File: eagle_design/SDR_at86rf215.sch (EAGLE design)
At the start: 221 parts, among them CON1 1734035-2, J1 SI-50170, J2 SJ-3523, J3 SMA0.062, J4 AMPHENOL_A-1JB, J5 5027740891, J6 AMPHENOL_A-1JB, J8 TC2030-CTX, Q1 MAR6-SM+, Q16 2N7002, SW1 45X45MM_TL3315, SW2 45X45MM_TL3315, SW3 45X45MM_TL3315, SW4 45X45MM_TL3315, SW5 45X45MM_TL3315, SW6 45X45MM_TL3315, SW7 45X45MM_TL3315, T1 0896FB15A0100, U1 AT86RF215, U10 NHD-C0216CZ-NSW-BBW-3V3, U11 MP34DT05TR-A, U12 ADP7156ARDZ-3.3-R7, U13 SN65LVDS1, U14 SN65LVDS1, U15 SN65LVDT2, U18 LAN8742, U2 ICE40HX8K-CT256, U3 TPS799X, U4 LD1117S12TR, U5 SN65LVDT2, U6 SN65LVDT2, U7 CS4344, U8 FT230XQ, U9 STM32H743ZIT6, X1 25MHz, X2 8MHZ, X3 ASVTX-12-A-40.000MHZ-H10-T

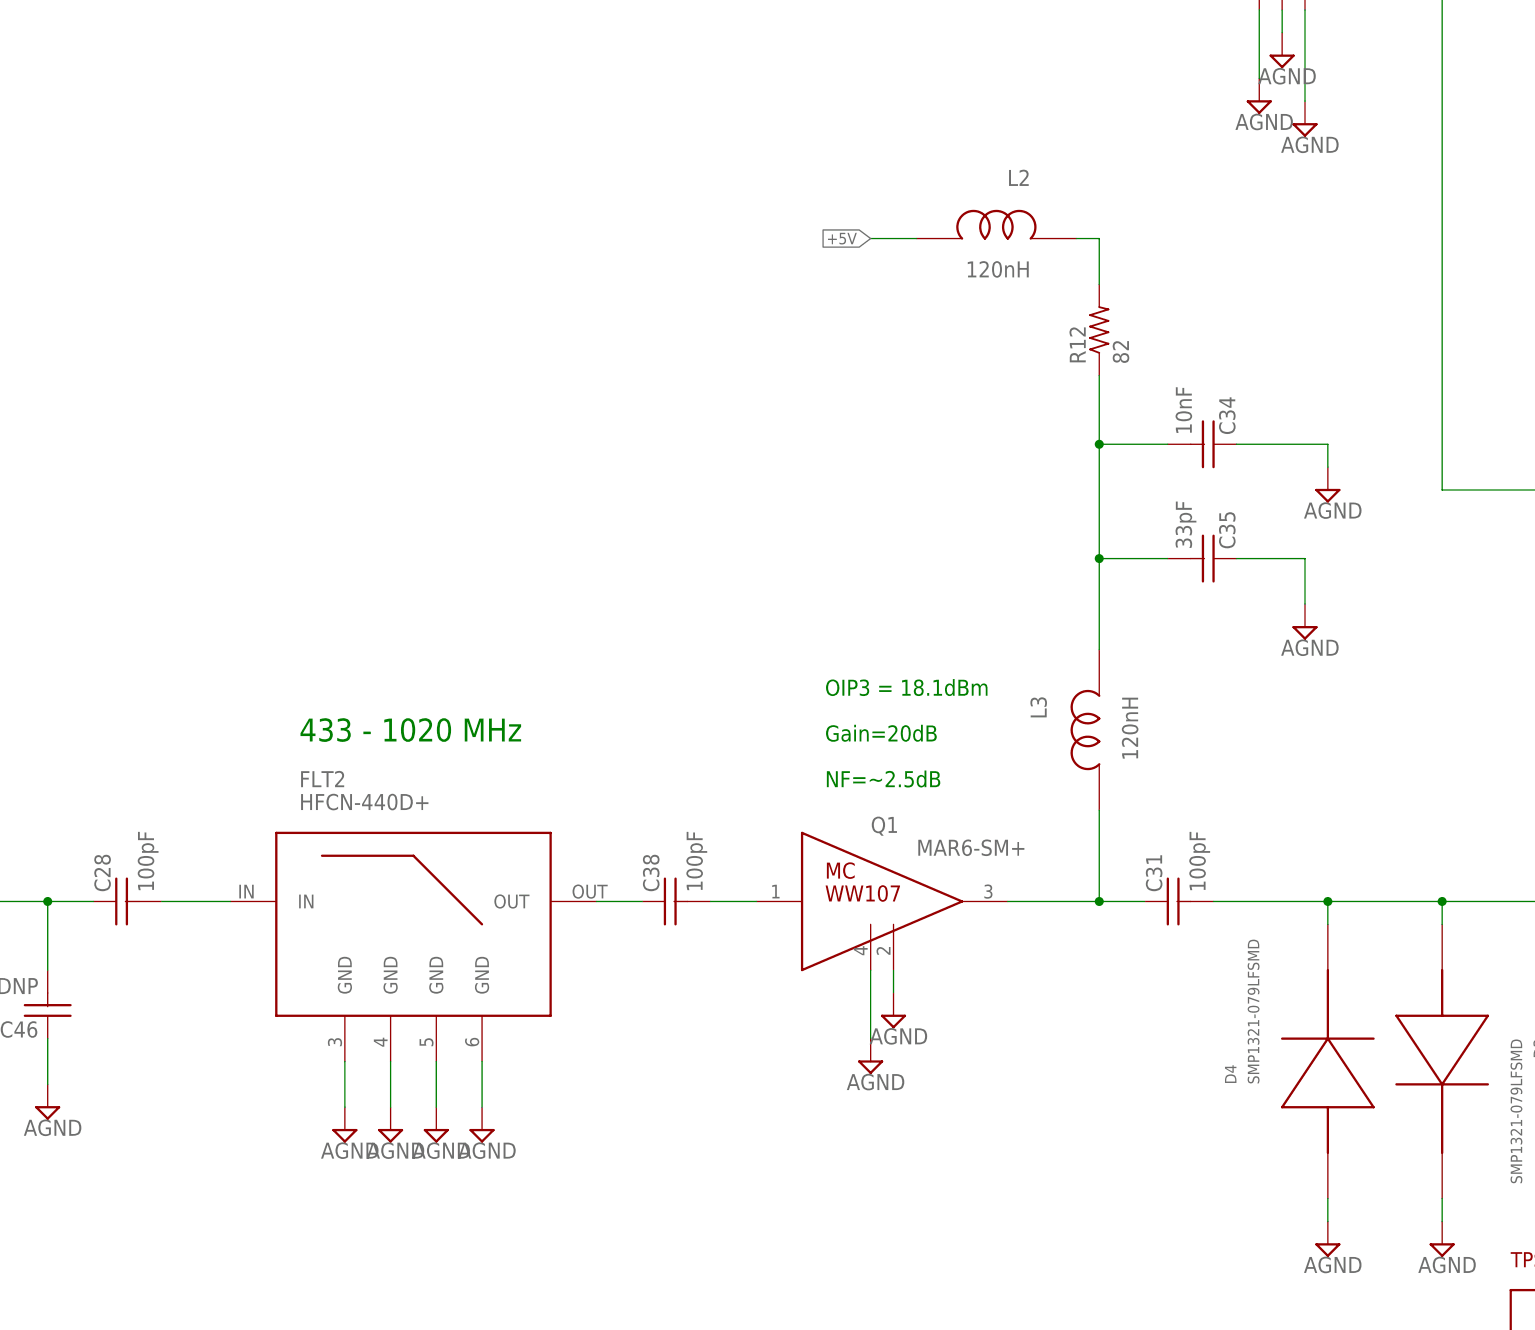
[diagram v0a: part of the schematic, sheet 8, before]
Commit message: update eagle files and schematic to reflect changes made to receiver when ext tuner was added
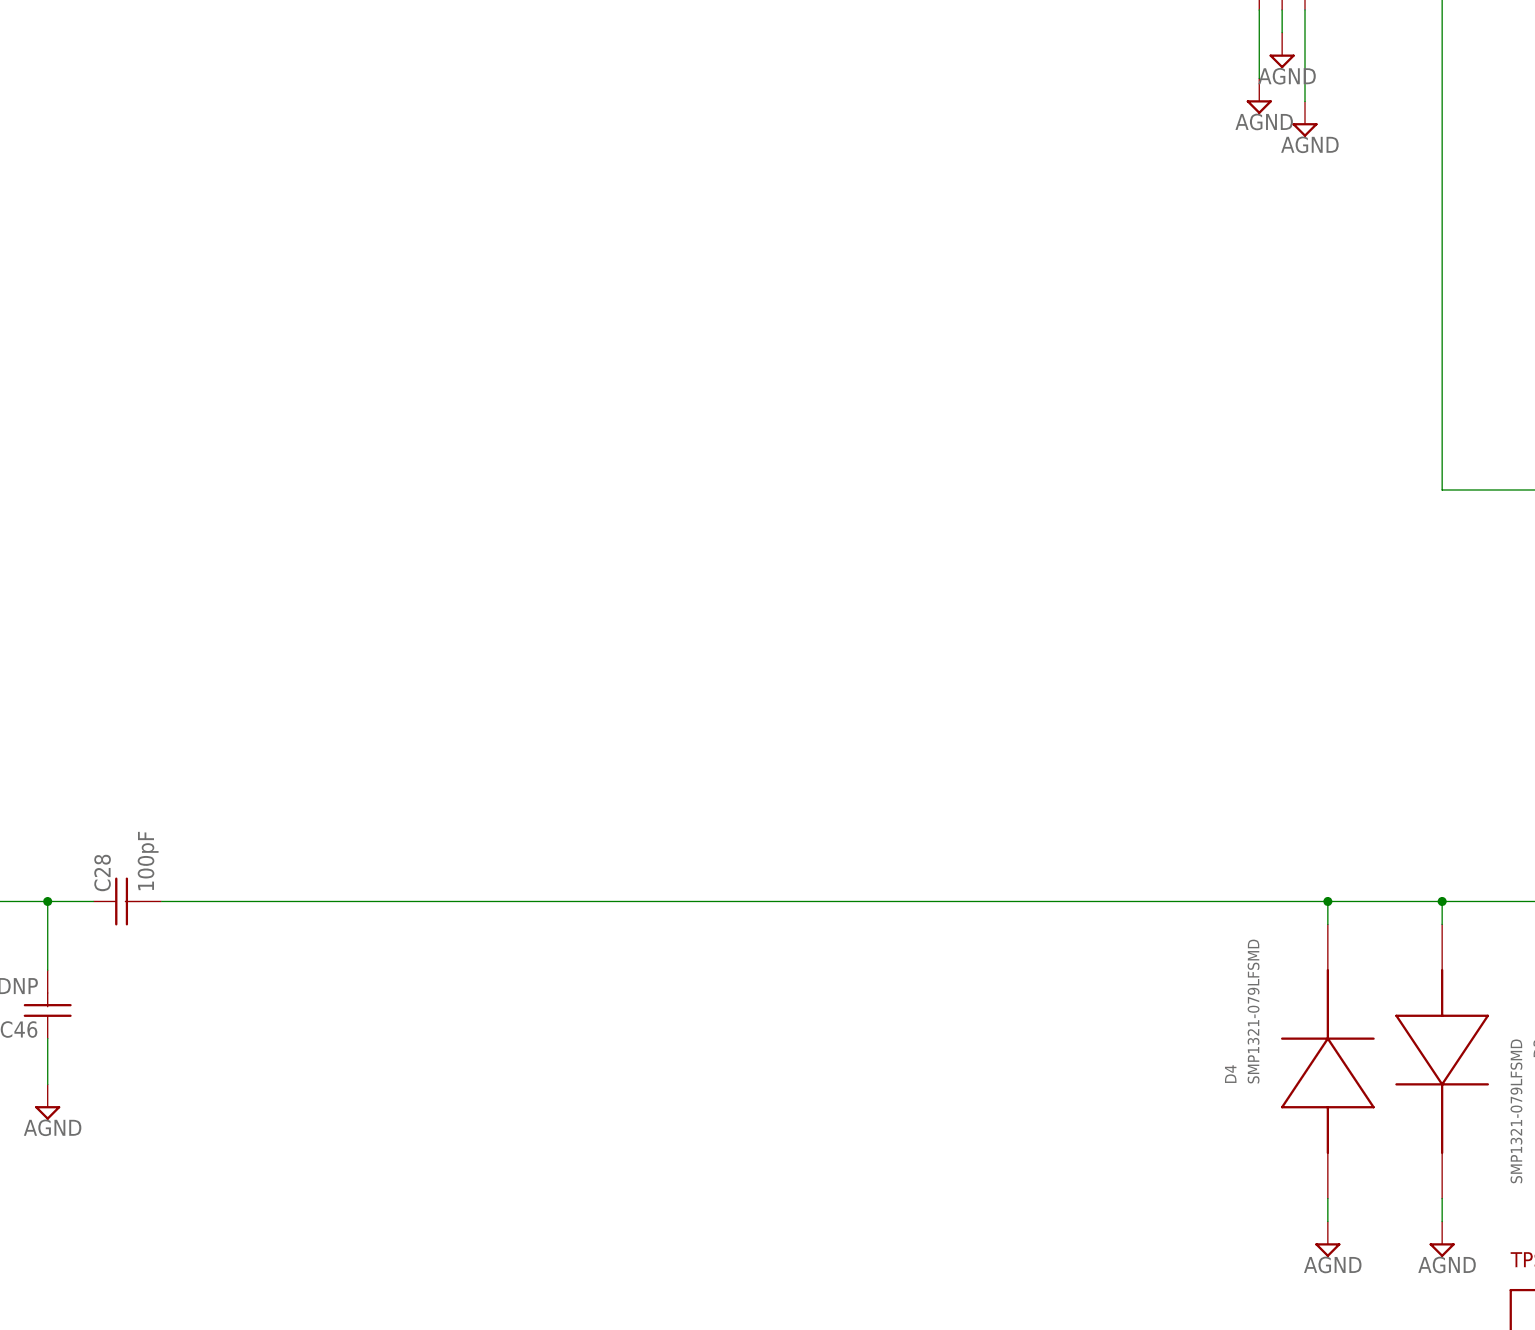
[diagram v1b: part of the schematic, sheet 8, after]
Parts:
- removed C31, C38: 100pF, m64library:C-USC0603
- removed C34: 10nF, m64library:C-USC0402
- removed C35: 33pF, m64library:C-USC0402
- removed FLT2: HFCN-440D+, 195_est_library:MINICIRCUITS_FV1206SMD
- removed L2, L3: 120nH, m64library:INDUCTORL0603
- removed Q1: MAR6-SM+, m64library:MAR-8ASM
- removed R12: 82, resistor:R-US_R1206
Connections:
- removed net N$18: C34.2, C35.2, L3.P$2, R12.1
- removed net N$19: C38.1, FLT2.OUT
- removed net N$21: C28.2, FLT2.IN
- removed net N$3: C38.2, Q1.1
- removed net N$44: L2.P$2, R12.2
- removed net N$45: C31.1, L3.P$1, Q1.3
- net +5V: no longer L2.P$1
- net GND: no longer C34.1, C35.1, FLT2.GND@1, FLT2.GND@2, FLT2.GND@3, FLT2.GND@4, Q1.2, Q1.4
- net N$46: now also C28.2; no longer C31.2
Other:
- note removed: "433 - 1020 MHz"
- note removed: "Gain=20dB"
- note removed: "NF=~2.5dB"
- note removed: "OIP3 = 18.1dBm"
